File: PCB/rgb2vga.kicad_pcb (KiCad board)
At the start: 2 copper layers, 81 x 55.9 mm, 40 parts, among them IC1 LM1881

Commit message: resistor values, routing
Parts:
- removed @HOLE0, @HOLE1: , 
- added R26: 3K, rgb2vga:0207_10, F.Cu at (160.4, 88.3)
- R1, R4: value 510 -> 750
- R10, R9: value 82 -> 47
- R2, R5: value 1K -> 1.5K
- R3, R6: value 2K -> 3K
- R7: value 390 -> 750
- R8: value 820 -> 1.5K
- moved C1 8.46 mm to (135.3, 86.4), turned to 90 degrees
- moved R9 8.14 mm to (153.0, 75.5)
- moved R10 8.14 mm to (153.0, 78.1)
- moved R7 8.14 mm to (153.0, 83.2)
- moved R8 8.14 mm to (153.0, 80.6)
- moved R3 8.13 mm to (153.0, 93.3)
- moved R6 8.13 mm to (153.0, 85.7)
- moved R2 8.13 mm to (153.0, 95.9)
- moved R4 8.13 mm to (153.0, 90.8)
- moved R5 8.13 mm to (153.0, 88.3)
- moved C2 6.96 mm to (130.8, 86.4), turned to 90 degrees
- moved R1 6.56 mm to (154.9, 98.4)
- moved R14 6.56 mm to (154.9, 116.2)
- moved R20 6.56 mm to (130.8, 125.1)
- moved R23 6.56 mm to (130.8, 79.4)
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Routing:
- net RSET: track 46.7 -> 40.2 mm
- net _HS: track 34.6 -> 40.0 mm
- net R0: track 20.6 -> 25.1 mm
- net (no net): track 0.00 -> 3.31 mm
- net R1: track 21.6 -> 24.7 mm
- net GREEN: track 22.6 -> 25.1 mm
- net BLUE: track 30.9 -> 33.3 mm
- net _VS: track 41.8 -> 44.1 mm
- net N$1: track 29.3 -> 27.3 mm
- net DIFFG: track 82.1 -> 80.1 mm
- net VSYNC: track 57.9 -> 59.8 mm
- net HS: track 19.5 -> 21.5 mm
- net VS: track 19.6 -> 21.5 mm
- net B0: track 20.6 -> 22.5 mm
- net B1: track 20.6 -> 22.5 mm
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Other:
- board size 81 x 55.9 mm -> 80.9 x 55.9 mm
- net class Default: trace_width 0.25 -> 0.2; via_dia 0.8 -> 0.6; via_drill 0.4 -> 0.3
- rule via_min_size: 0.4 -> 0.5
- board text added: "DE0-NANO RGB2VGA"
- board text added: "Original Design 2014 Luis Antoniosi"
- board text added: "github.com/bkw777/rgb2vga - v002"
- board text removed: "2014 LUIS ANTONIOSI V1R0"
- board text removed: "ALTERA"
- board text removed: "CONVERTER"
- board text removed: "DE0-NANO"
- board text removed: "RGB2VGA"

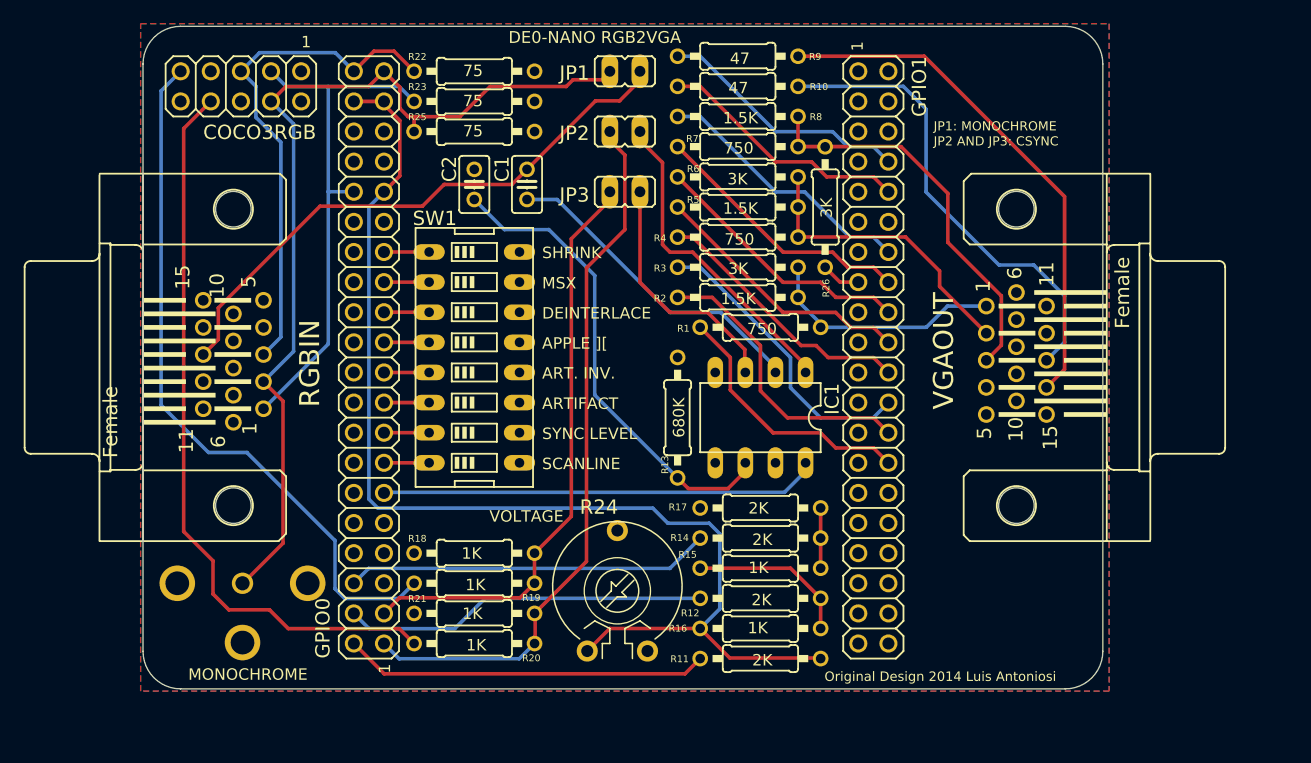
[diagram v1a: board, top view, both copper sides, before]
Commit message: recreated schematic, add rgbi resistors, 3d models, digikey bom, Roger Taylor resistor values
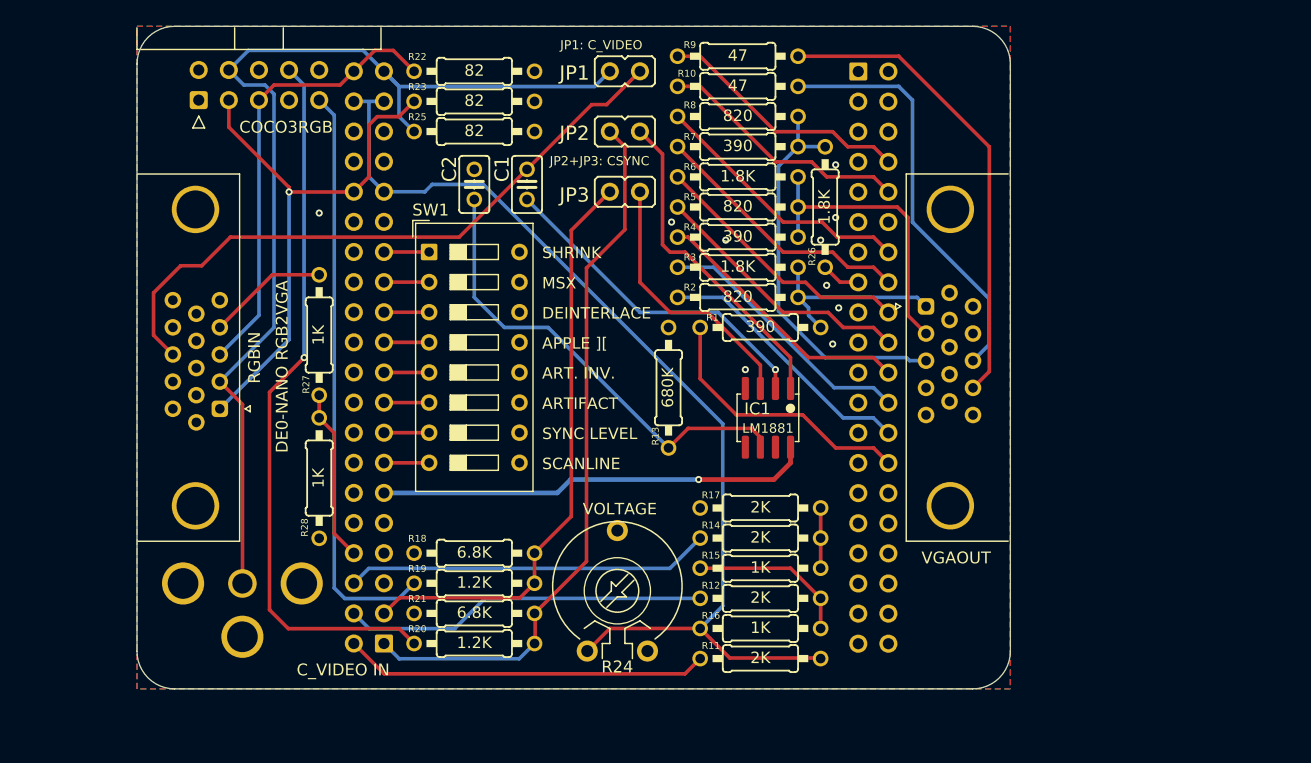
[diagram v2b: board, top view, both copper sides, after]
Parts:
- removed the COCO3RGB at (111.1, 78.1)
- added COCO3RGB: , 000_LOCAL:IDC-Header_2x05_P2.54mm_Horizontal, F.Cu at (107.6, 79.2)
- added R27: 1K, 000_LOCAL:0207_10, F.Cu at (117.7, 99.1)
- added R28: 1K, 000_LOCAL:0207_10, F.Cu at (117.7, 111.1)
- C1, C2: footprint rgb2vga:C025-025X050 -> 000_LOCAL:C025-025X050
- GPIO0, GPIO1: footprint rgb2vga:2X20 -> 000_LOCAL:PinSocket_2x20_P2.54mm_Vertical; moved to B.Cu
- IC1: footprint rgb2vga:DIL08 -> 000_LOCAL:SOIC-8_4x5
- JP1, JP2, JP3: footprint rgb2vga:JP1 -> 000_LOCAL:JP
- R1, R4, R7: value 750 -> 390; footprint rgb2vga:0207_10 -> 000_LOCAL:0207_10
- R10, R11, R12, R13, R14, R15, R16, R17, R9: footprint rgb2vga:0207_10 -> 000_LOCAL:0207_10
- R18, R21: value 1K -> 6.8K; footprint rgb2vga:0207_10 -> 000_LOCAL:0207_10
- R19, R20: value 1K -> 1.2K; footprint rgb2vga:0207_10 -> 000_LOCAL:0207_10
- R2, R5, R8: value 1.5K -> 820; footprint rgb2vga:0207_10 -> 000_LOCAL:0207_10
- R22, R23, R25: value 75 -> 82; footprint rgb2vga:0207_10 -> 000_LOCAL:0207_10
- R24: footprint rgb2vga:PT-10 -> 000_LOCAL:PT-10
- R26, R3, R6: value 3K -> 1.8K; footprint rgb2vga:0207_10 -> 000_LOCAL:0207_10
- RGBIN, VGAOUT: footprint rgb2vga:HDF15H -> 000_LOCAL:DSUB-15-HD_Female_Horizontal_P2.29x1.98mm_EdgePinOffset3.03mm_Housed_MountingHolesOffset4.94mm
- SW1: footprint rgb2vga:EDG-08 -> 000_LOCAL:SW_DIP_SPSTx08_Slide_9.78x22.5mm_W7.62mm_P2.54mm
- U$1: footprint rgb2vga:RCA -> 000_LOCAL:RCA
- moved GPIO0 24.2 mm to (123.2, 125.1), turned to 0 degrees
- moved GPIO1 24.1 mm to (163.2, 76.8), turned to 180 degrees
- moved SW1 9.67 mm to (127.0, 92.1), turned to 0 degrees
- moved VGAOUT 8.75 mm to (168.9, 96.6)
- moved RGBIN 4.48 mm to (109.3, 105.3)
- moved R13 2.64 mm to (147.2, 103.5), turned to 90 degrees
- moved IC1 0.63 mm to (155.6, 106.0), turned to 270 degrees
- moved U$1 0.51 mm to (111.3, 120.0)
- turned R1 to 0 degrees
- turned R10 to 0 degrees
- turned R11 to 0 degrees
- turned R12 to 0 degrees
- turned R14 to 0 degrees
- turned R19 to 0 degrees
- turned R2 to 0 degrees
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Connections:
- R1 pad 1: RED -> R2
- R1 pad 2: R2 -> RED
- R10 pad 1: _HS -> HS
- R10 pad 2: HS -> _HS
- R11 pad 1: DIFF_N -> D2
- R11 pad 2: D2 -> DIFF_N
- R12 pad 1: N$6 -> D1
- R12 pad 2: D1 -> N$6
- R13 pad 1: GND -> RSET
- R13 pad 2: RSET -> GND
- R14 pad 1: N$4 -> D0
- R14 pad 2: D0 -> N$4
- R19 pad 1: _VSYNC -> VSYNC
- R19 pad 2: VSYNC -> _VSYNC
- R2 pad 1: RED -> R1
- R2 pad 2: R1 -> RED
- R20 pad 1: _HSYNC -> HSYNC
- R20 pad 2: HSYNC -> _HSYNC
- R24 pad 2: (no net) -> GND
- R24 pad 3: GND -> (no net)
- R3 pad 1: RED -> R0
- R3 pad 2: R0 -> RED
- R4 pad 1: GREEN -> G2
- R4 pad 2: G2 -> GREEN
- R5 pad 1: GREEN -> G1
- R5 pad 2: G1 -> GREEN
- R6 pad 1: GREEN -> G0
- R6 pad 2: G0 -> GREEN
- R7 pad 1: BLUE -> B1
- R7 pad 2: B1 -> BLUE
- R8 pad 1: BLUE -> B0
- R8 pad 2: B0 -> BLUE
- R9 pad 1: _VS -> VS
- R9 pad 2: VS -> _VS
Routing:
- net (no net): track 3.31 -> 28.1 mm
- net DIFF_N: track 98.7 -> 87.5 mm
- net VSYNC: track 59.8 -> 49.3 mm
- net DIFFG: track 80.1 -> 89.4 mm
- net CSYNC: track 48.7 -> 54.6 mm
- net DIFFB: track 43.2 -> 38.4 mm
- net _HS: track 40.0 -> 35.4 mm
- net _VS: track 44.1 -> 40.2 mm
- net RED: track 20.6 -> 17.0 mm
- net R0: track 25.1 -> 22.5 mm
- net R1: track 24.7 -> 22.5 mm
- net DIFFR: track 44.7 -> 46.9 mm, vias 0 -> 1
- net N$2: track 20.8 -> 22.7 mm
- net HSYNC: track 62.2 -> 60.6 mm, vias 0 -> 1
- net N$1: track 27.3 -> 28.5 mm, vias 0 -> 1
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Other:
- board size 80.9 x 55.9 mm -> 73.7 x 55.9 mm
- board text added: "AUDIO"
- board text added: "B"
- board text added: "C_VIDEO IN"
- board text added: "G"
- board text added: "GND"
- board text added: "H"
- board text added: "JP1: C_VIDEO"
- board text added: "JP2+JP3: CSYNC"
- board text added: "PB3"
- board text added: "R"
- board text added: "V"
- board text added: "github.com/bkw777/rgb2vga - v003"
- board text removed: "1"
- board text removed: "JP1: MONOCHROME"
- board text removed: "JP2 AND JP3: CSYNC"
- board text removed: "MONOCHROME"
- board text removed: "github.com/bkw777/rgb2vga - v002"

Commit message: add some net labels and fix several errors in the schematic didn't match the pcb
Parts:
- C_VIDEO_IN: renamed from U$1; value RCA-CINCH -> RCA female 90 degree

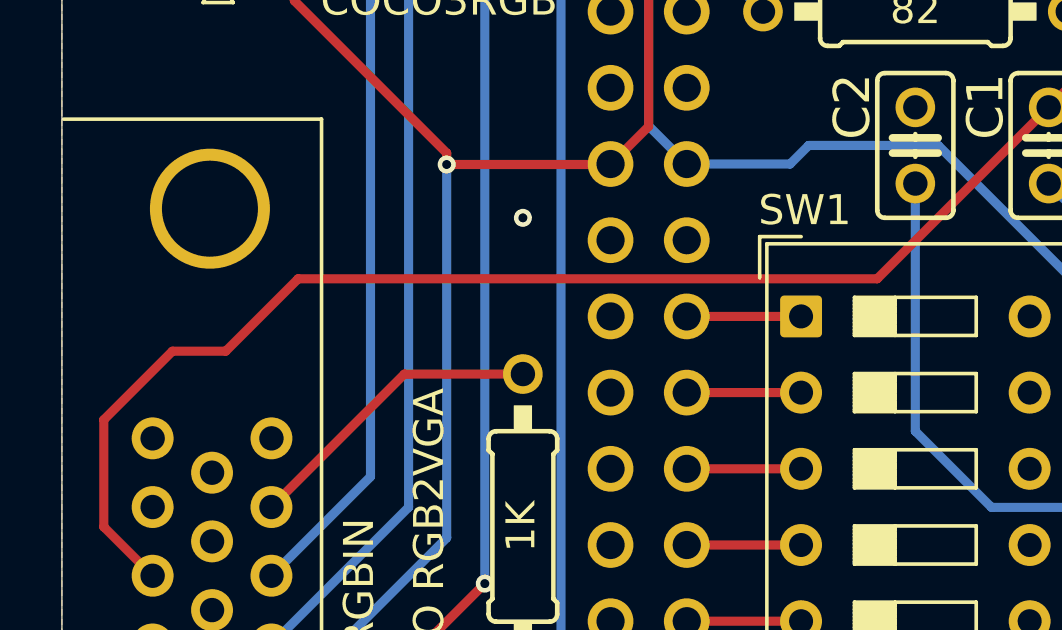
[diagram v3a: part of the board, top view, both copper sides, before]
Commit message: spread schematic out a little
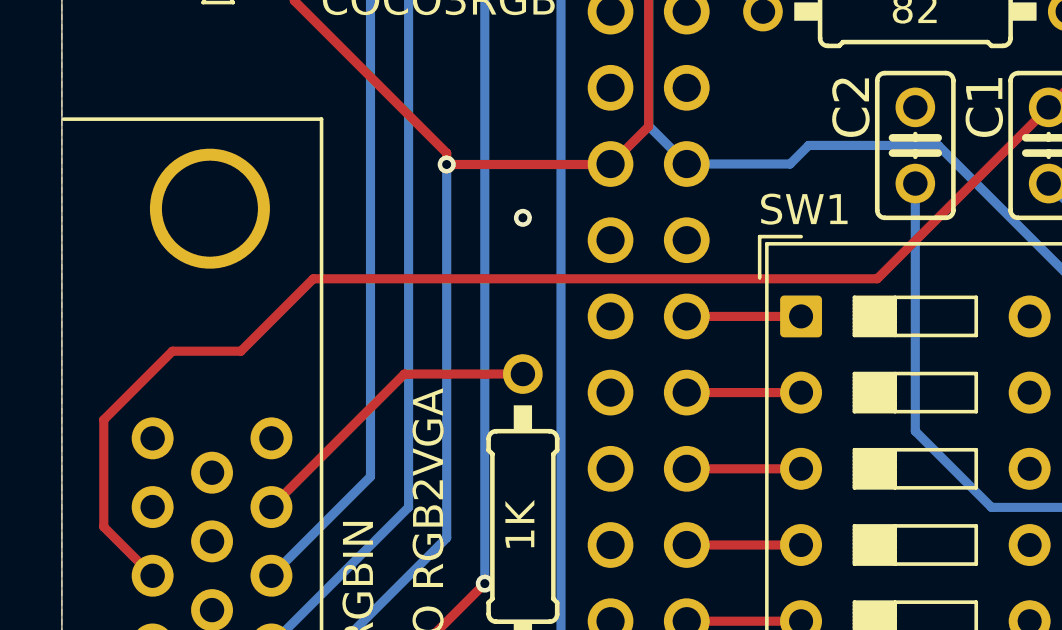
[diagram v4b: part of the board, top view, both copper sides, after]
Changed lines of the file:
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@@
   (segment (start 141.9707 79.629) (end 140.716 79.629) (width 0.3048) (layer Top) (net 28))
   (segment (start 144.7811 76.8186) (end 141.9707 79.629) (width 0.3048) (layer Top) (net 28))
-  (segment (start 103.759 99.075) (end 105.387 100.703) (width 0.3048) (layer Top) (net 28))
   (segment (start 103.759 95.504) (end 103.759 99.075) (width 0.3048) (layer Top) (net 28))
   (segment (start 106.045 93.218) (end 103.759 95.504) (width 0.3048) (layer Top) (net 28))
-  (segment (start 107.823 93.218) (end 106.045 93.218) (width 0.3048) (layer Top) (net 28))
-  (segment (start 110.236 90.805) (end 107.823 93.218) (width 0.3048) (layer Top) (net 28))
-  (segment (start 129.54 90.805) (end 110.236 90.805) (width 0.3048) (layer Top) (net 28))
+  (segment (start 103.759 99.075) (end 105.387 100.703) (width 0.3048) (layer Top) (net 28))
+  (segment (start 108.331 93.218) (end 106.045 93.218) (width 0.3048) (layer Top) (net 28))
+  (segment (start 110.744 90.805) (end 108.331 93.218) (width 0.3048) (layer Top) (net 28))
+  (segment (start 129.54 90.805) (end 110.744 90.805) (width 0.3048) (layer Top) (net 28))
   (segment (start 135.255 85.09) (end 129.54 90.805) (width 0.3048) (layer Top) (net 28))
   (segment (start 148.844 106.934) (end 147.193 108.585) (width 0.3048) (layer Top) (net 29))
@@
     (connect_pads (clearance 0.2))
     (min_thickness 0.2)
-    (fill (arc_segments 32) (thermal_gap 0.2) (thermal_bridge_width 0.4) (smoothing fillet) (radius 0.1))
+    (fill yes (arc_segments 32) (thermal_gap 0.2) (thermal_bridge_width 0.4) (smoothing fillet) (radius 0.1))
     (polygon
       (pts
@@
     (connect_pads (clearance 0.2))
     (min_thickness 0.2)
-    (fill (arc_segments 32) (thermal_gap 0.2) (thermal_bridge_width 0.4) (smoothing fillet) (radius 0.1))
+    (fill yes (arc_segments 32) (thermal_gap 0.2) (thermal_bridge_width 0.4) (smoothing fillet) (radius 0.1))
     (polygon
       (pts

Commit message: net labels
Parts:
- renumbered COCO3RGB to COCO3_RGB_IN, RGBIN to RGB_IN, IC1 to U1, VGAOUT to VGA_OUT

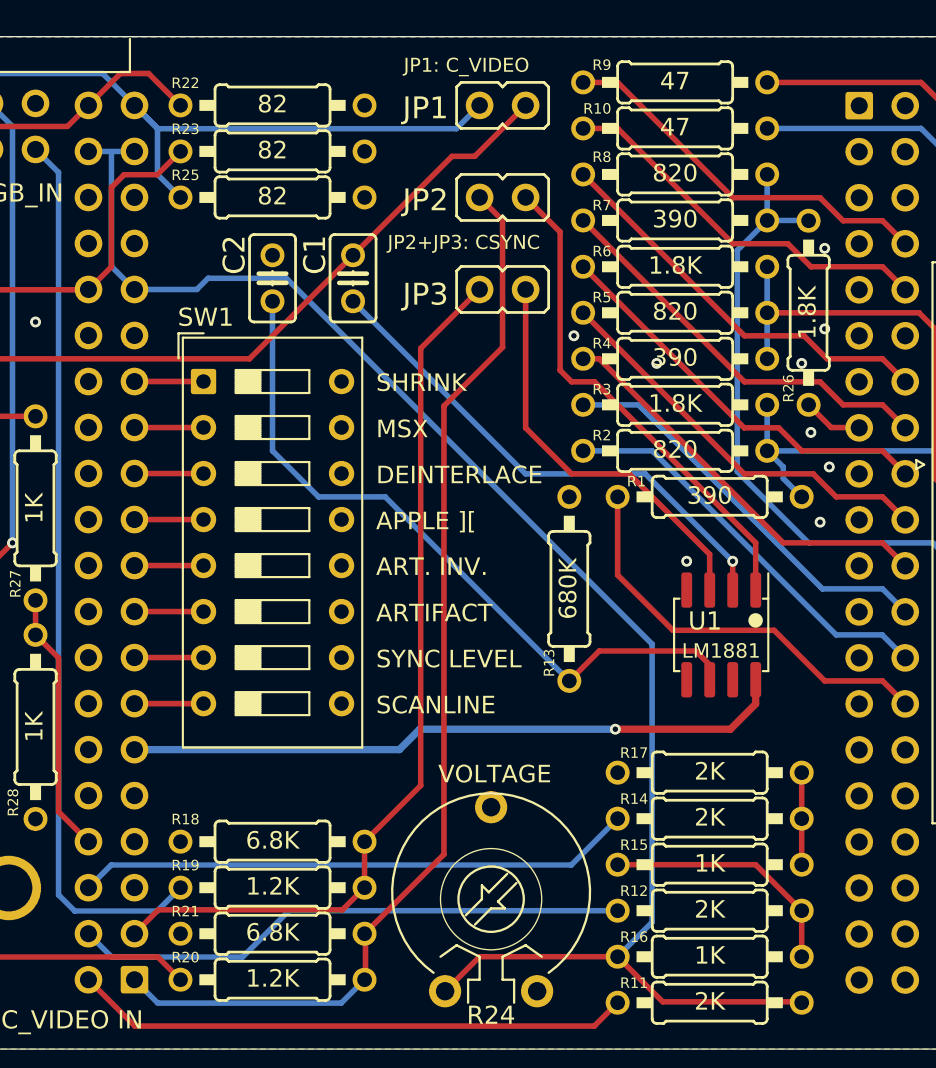
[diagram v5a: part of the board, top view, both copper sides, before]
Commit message: move caps near lm1881
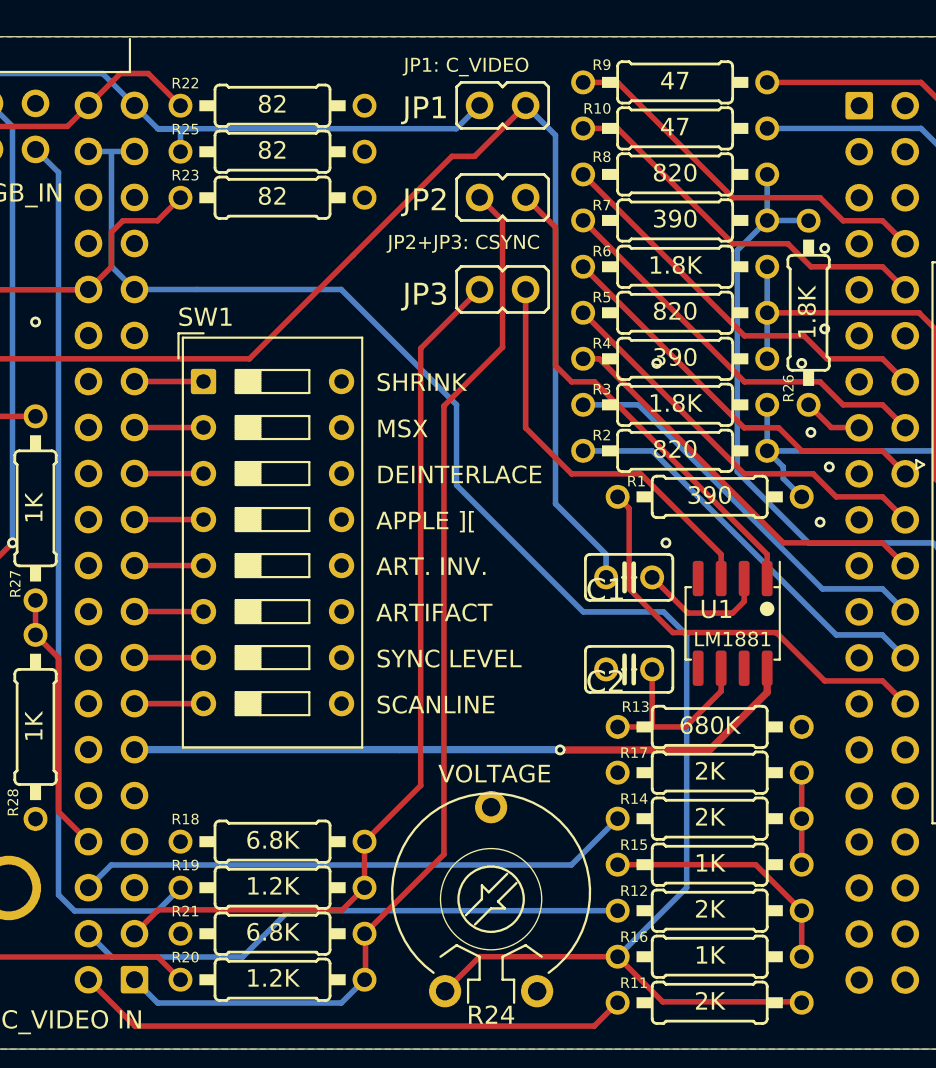
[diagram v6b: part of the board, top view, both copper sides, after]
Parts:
- moved C2 29.2 mm to (150.5, 108.0), turned to 180 degrees
- moved C1 22.5 mm to (150.5, 102.9), turned to 180 degrees
- moved R13 10.9 mm to (154.9, 111.1), turned to 0 degrees
- moved R23 2.56 mm to (130.8, 81.9)
- moved R25 2.52 mm to (130.8, 79.4)
- moved U1 0.90 mm to (156.2, 105.4)
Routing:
- net RSET: track 39.5 -> 11.0 mm
- net CSYNC: track 54.6 -> 82.5 mm
- net N$1: track 28.5 -> 7.43 mm, vias 1 -> 0
- net DIFF_N: track 87.5 -> 92.5 mm
- net DIFFG: track 89.4 -> 85.7 mm
- net DIFFR: track 46.9 -> 44.3 mm
- net VCC: track 36.7 -> 37.6 mm
- net GND: vias 10 -> 9
